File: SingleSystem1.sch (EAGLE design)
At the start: 7 parts, among them U2 SD_CARD_SOCKET, U3 XBEE

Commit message: done, now verifying
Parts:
- added 12+, GND: SE14, solpad:SE14
- added 3.3V, 5V, 9V: (no value), con-amp-quick:M02
- added 3DR: 653006114822, Wire_to_Board_Connectors_rev15d:653006114822
- added 5REG, 9REG: V_REG_317SMD, SparkFun-PowerIC:V_REG_317SMD
- added A1_FTDI, A2_FTDI, GPS_FTDI, IMU_FTDI: (no value), con-amp-quick:M06
- added ANEMOMETER1, ANEMOMETER2: 61200622323, Wurth_Elektronik_Electromechanic_Wire_to_Board_Connectors_rev15c:61200622323
- added C1, C3: 1uF, SparkFun-Capacitors:1UF-25V-10%(0805)
- added C13, C15: 0.1UF, SparkFun-Capacitors:1UF-25V-10%(0805)
- added C14, C16: 1UF, SparkFun-Capacitors:1UF-25V-10%(0805)
- added C2: 100uF, SparkFun-Capacitors:CAP1206
- added C4: 10uF, SparkFun-Capacitors:CAP0805
- added C5, C9: 0.022uF, SparkFun-Capacitors:CAP0603-CAP
- added D2: (no value), Wuerth_Elektronik_LEDs_rev15b:WL-SMCW-150120BS75000-B
- added R13: 68.1k, resistor:R-US_M2012
- added R17: 100k, resistor:R-US_M2012
- added R2: (no value), resistor:R-US_M2012
- added R3: 750 ohms, adafruit:R-US_M2012
- added R4, R6: 240 ohms, adafruit:R-US_M2012
- added R5: 1.5k, adafruit:R-US_M2012
- added R7: 1.07k, resistor:R-US_M2012
- added R8: 5.62k, resistor:R-US_M2012
- added R9: 11.8k, resistor:R-US_M2012
- added U1: LMZ14203, SparkFun-PowerIC:LMZ14203
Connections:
- new net +12V: 12+.MP, 9REG.IN, C1.1, C15.1, C4.1, D2.A, R13.2, R17.2, U1.VIN
- new net +9V: 5REG.IN, 9REG.OUT, 9V.2, C13.1, C16.1, R6.2, U$1.VIN
- new net 3DR_RX: 3DR.3
- new net 3DR_TX: 3DR.2
- new net A1_PWR: ANEMOMETER1.2
- new net A2_PWR: ANEMOMETER2.2
- new net N$2: 5REG.ADJ, R3.2, R4.1
- new net N$3: 9REG.ADJ, R5.2, R6.1
- new net N$4: R13.1, R9.2, U1.EN
- new net N$5: R17.1, U1.RON
- new net N$6: C9.1, U1.SS
- new net N$7: D2.K, R2.2
- new net N$8: C5.1, R7.2, R8.2, U1.FB
- net +5V: now also 3DR.1, 5REG.OUT, 5V.2, C14.1, R4.2
- net 3.3V: now also 3.3V.2, C2.1, C3.1, C5.2, R8.1, U1.VOUT
- net A1_IN_RX: now also ANEMOMETER1.5
- net A1_IN_TX: now also ANEMOMETER1.3
- net A1_RX: now also A1_FTDI.2
- net A1_TX: now also A1_FTDI.3
- net A2_IN_RX: now also ANEMOMETER2.5
- net A2_IN_TX: now also ANEMOMETER2.3
- net A2_RX: now also A2_FTDI.2
- net A2_TX: now also A2_FTDI.3
- net GND: now also 3.3V.1, 3DR.6, 5V.1, 9V.1, A1_FTDI.6, A2_FTDI.6, ANEMOMETER1.1, ANEMOMETER1.4, ANEMOMETER2.1, ANEMOMETER2.4, C1.2, C13.2, C14.2, C15.2, C16.2, C2.2, C3.2, C4.2, C9.2, GND.MP, GPS_FTDI.6, IMU_FTDI.6, R2.1, R3.1, R5.1, R7.1, R9.1, U$1.5V, U1.EP, U1.GND
- net GPS_RX: now also GPS_FTDI.3, U$1.52
- net GPS_TX: now also GPS_FTDI.2, U$1.A11
- net IMU_RX: now also IMU_FTDI.3
- net IMU_TX: now also IMU_FTDI.2

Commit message: Done, Kanishke will verify
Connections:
- net GND: now also U$1.GND_1; no longer U$1.5V
- net GPS_RX: now also U$1.A11; no longer U$1.52
- net GPS_TX: now also U$1.52; no longer U$1.A11
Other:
- moved on the sheet: GPS(OEM615), IMUCONNECTION, MAX232_1, MAX232_2, U2, U3

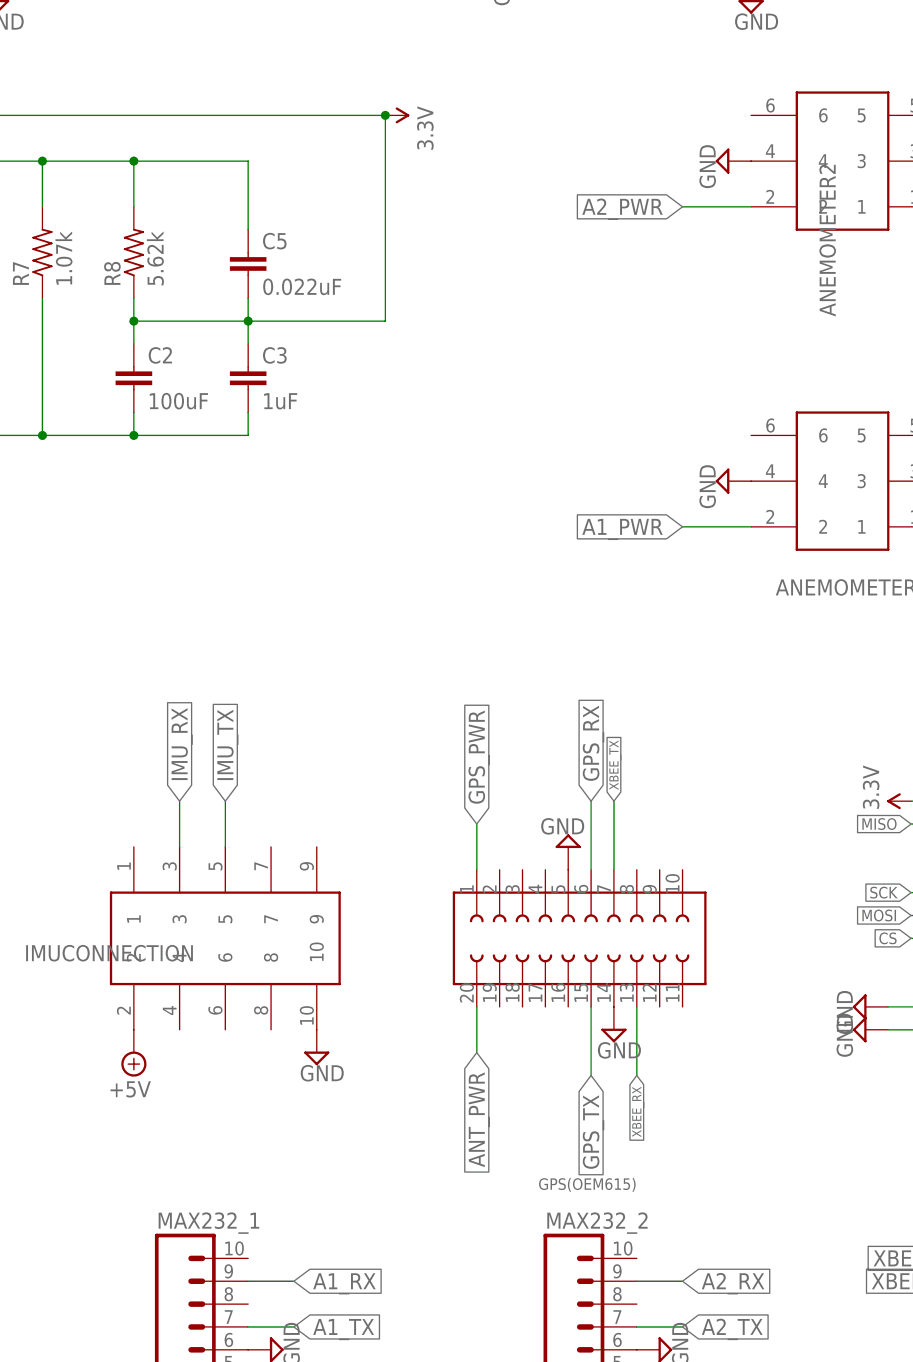
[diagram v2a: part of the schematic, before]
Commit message: edited the pwr connections
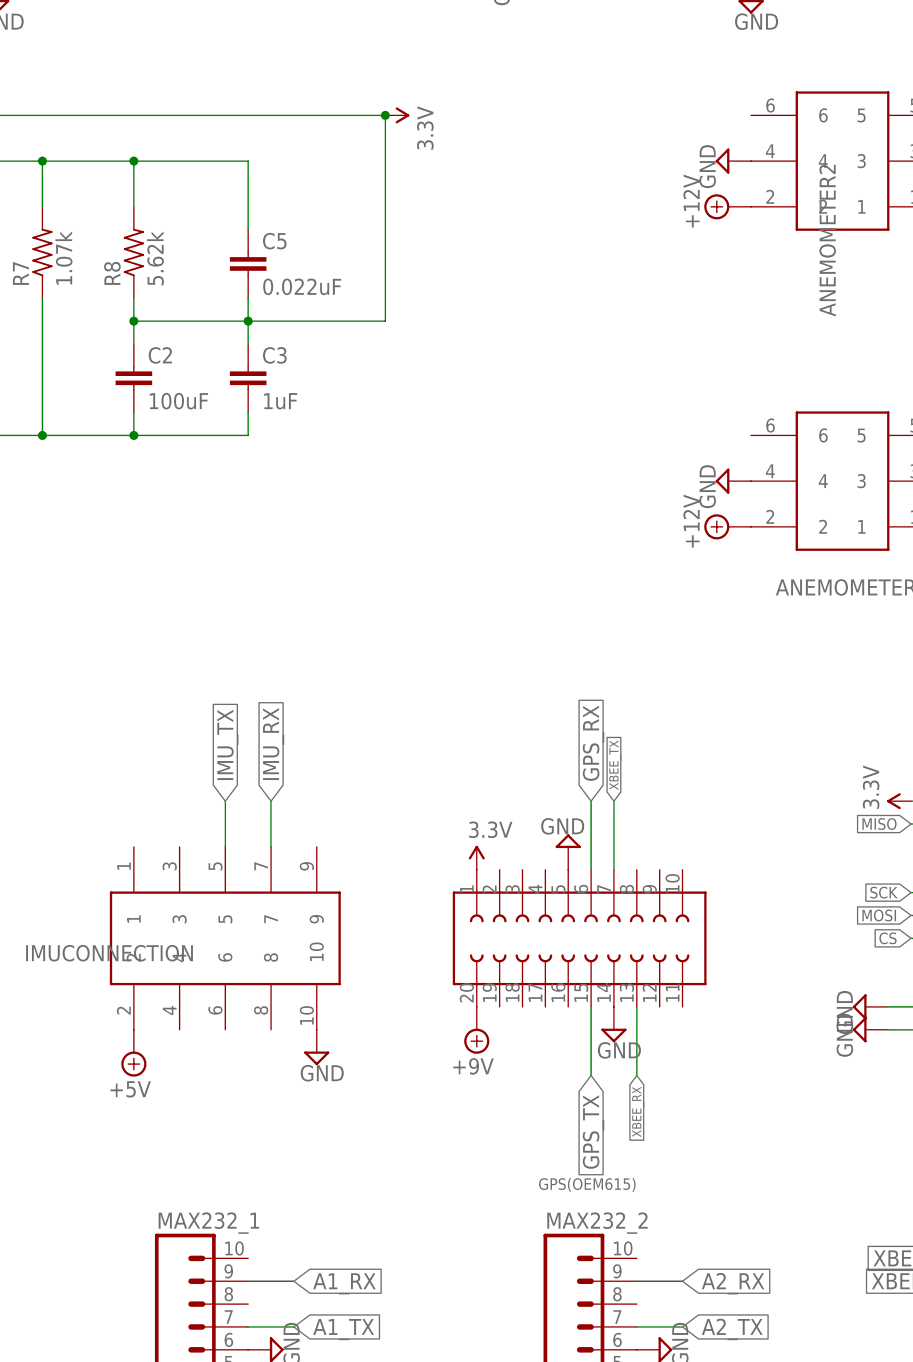
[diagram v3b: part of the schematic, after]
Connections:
- removed net A1_PWR: ANEMOMETER1.2
- removed net A2_PWR: ANEMOMETER2.2
- removed net ANT_PWR: GPS(OEM615).20
- removed net GPS_PWR: GPS(OEM615).1
- net +12V: now also ANEMOMETER1.2, ANEMOMETER2.2
- net +9V: now also GPS(OEM615).20
- net 3.3V: now also GPS(OEM615).1
- net IMU_RX: now also IMUCONNECTION.7; no longer IMUCONNECTION.3
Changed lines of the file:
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@@
 <part name="SUPPLY2" library="supply2" deviceset="+9V" device=""/>
 <part name="SUPPLY5" library="supply2" deviceset="GND" device=""/>
+<part name="SUPPLY6" library="supply2" deviceset="+9V" device=""/>
+<part name="SUPPLY7" library="SparkFun-Aesthetics" deviceset="3.3V" device=""/>
+<part name="SUPPLY10" library="supply2" deviceset="+12V" device=""/>
+<part name="SUPPLY17" library="supply2" deviceset="+12V" device=""/>
 </parts>
 <sheets>
@@
 <instance part="SUPPLY2" gate="G$1" x="2.54" y="15.24" rot="R90"/>
 <instance part="SUPPLY5" gate="GND" x="2.54" y="20.32" rot="R270"/>
+<instance part="SUPPLY6" gate="G$1" x="142.24" y="68.58" rot="R180"/>
+<instance part="SUPPLY7" gate="G$1" x="142.24" y="86.36"/>
+<instance part="SUPPLY10" gate="+12V" x="170.18" y="160.02" rot="R90"/>
+<instance part="SUPPLY17" gate="+12V" x="170.18" y="124.46" rot="R90"/>
 </instances>
 <busses>
@@
 <net name="IMU_RX" class="0">
 <segment>
-<pinref part="IMUCONNECTION" gate="G$1" pin="3"/>
-<wire x1="109.22" y1="88.9" x2="109.22" y2="93.98" width="0.1524" layer="91"/>
-<label x="109.22" y="93.98" size="1.778" layer="95" rot="R90" xref="yes"/>
-</segment>
-<segment>
 <pinref part="U$1" gate="G$1" pin="TX3"/>
 <wire x1="5.08" y1="68.58" x2="0" y2="68.58" width="0.1524" layer="91"/>
@@
 <label x="45.72" y="248.92" size="1.778" layer="95" xref="yes"/>
 </segment>
+<segment>
+<pinref part="IMUCONNECTION" gate="G$1" pin="7"/>
+<wire x1="119.38" y1="88.9" x2="119.38" y2="93.98" width="0.1524" layer="91"/>
+<label x="119.38" y="93.98" size="1.778" layer="95" rot="R90" xref="yes"/>
+</segment>
 </net>
 <net name="IMU_TX" class="0">
+<segment>
+<pinref part="U$1" gate="G$1" pin="RX3"/>
+<wire x1="5.08" y1="66.04" x2="0" y2="66.04" width="0.1524" layer="91"/>
+<label x="0" y="66.04" size="1.778" layer="95" rot="R180" xref="yes"/>
+</segment>
+<segment>
+<pinref part="IMU_FTDI" gate="G$1" pin="2"/>
+<wire x1="35.56" y1="246.38" x2="45.72" y2="246.38" width="0.1524" layer="91"/>
+<label x="45.72" y="246.38" size="1.778" layer="95" xref="yes"/>
+</segment>
 <segment>
 <pinref part="IMUCONNECTION" gate="G$1" pin="5"/>
@@
 <label x="114.3" y="93.98" size="1.778" layer="95" rot="R90" xref="yes"/>
 </segment>
-<segment>
-<pinref part="U$1" gate="G$1" pin="RX3"/>
-<wire x1="5.08" y1="66.04" x2="0" y2="66.04" width="0.1524" layer="91"/>
-<label x="0" y="66.04" size="1.778" layer="95" rot="R180" xref="yes"/>
-</segment>
-<segment>
-<pinref part="IMU_FTDI" gate="G$1" pin="2"/>
-<wire x1="35.56" y1="246.38" x2="45.72" y2="246.38" width="0.1524" layer="91"/>
-<label x="45.72" y="246.38" size="1.778" layer="95" xref="yes"/>
-</segment>
 </net>
 <net name="XBEE_TX" class="0">
@@
 <pinref part="U3" gate="G$1" pin="DIN"/>
 <label x="198.12" y="40.64" size="1.778" layer="95" rot="R180" xref="yes"/>
-</segment>
-</net>
-<net name="GPS_PWR" class="0">
-<segment>
-<pinref part="GPS(OEM615)" gate="G$1" pin="1"/>
-<wire x1="142.24" y1="86.36" x2="142.24" y2="91.44" width="0.1524" layer="91"/>
-<label x="142.24" y="91.44" size="1.778" layer="95" rot="R90" xref="yes"/>
-</segment>
-</net>
-<net name="ANT_PWR" class="0">
-<segment>
-<pinref part="GPS(OEM615)" gate="G$1" pin="20"/>
-<wire x1="142.24" y1="71.12" x2="142.24" y2="66.04" width="0.1524" layer="91"/>
-<label x="142.24" y="66.04" size="1.778" layer="95" rot="R270" xref="yes"/>
 </segment>
 </net>
@@
 <pinref part="3.3V" gate="G$1" pin="2"/>
 <pinref part="SUPPLY22" gate="G$1" pin="3.3V"/>
+</segment>
+<segment>
+<pinref part="GPS(OEM615)" gate="G$1" pin="1"/>
+<pinref part="SUPPLY7" gate="G$1" pin="3.3V"/>
 </segment>
 </net>
@@
 <pinref part="SUPPLY21" gate="+12V" pin="+12V"/>
 </segment>
+<segment>
+<pinref part="ANEMOMETER2" gate="G$1" pin="2"/>
+<pinref part="SUPPLY10" gate="+12V" pin="+12V"/>
+</segment>
+<segment>
+<pinref part="ANEMOMETER1" gate="G$1" pin="2"/>
+<pinref part="SUPPLY17" gate="+12V" pin="+12V"/>
+</segment>
 </net>
 <net name="N$4" class="0">
@@
 <pinref part="SUPPLY2" gate="G$1" pin="+9V"/>
 </segment>
+<segment>
+<pinref part="GPS(OEM615)" gate="G$1" pin="20"/>
+<pinref part="SUPPLY6" gate="G$1" pin="+9V"/>
+</segment>
 </net>
 <net name="N$2" class="0">
@@
 </segment>
 </net>
-<net name="A1_PWR" class="0">
-<segment>
-<pinref part="ANEMOMETER1" gate="G$1" pin="2"/>
-<wire x1="172.72" y1="124.46" x2="165.1" y2="124.46" width="0.1524" layer="91"/>
-<label x="165.1" y="124.46" size="1.778" layer="95" rot="R180" xref="yes"/>
-</segment>
-</net>
-<net name="A2_PWR" class="0">
-<segment>
-<pinref part="ANEMOMETER2" gate="G$1" pin="2"/>
-<wire x1="172.72" y1="160.02" x2="165.1" y2="160.02" width="0.1524" layer="91"/>
-<label x="165.1" y="160.02" size="1.778" layer="95" rot="R180" xref="yes"/>
-</segment>
-</net>

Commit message: edited 3DR
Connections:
- net 3DR_RX: now also U$1.TX0
- net 3DR_TX: now also U$1.RX0
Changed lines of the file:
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@@
 <wire x1="33.02" y1="208.28" x2="33.02" y2="198.12" width="0.1524" layer="91"/>
+</segment>
+<segment>
+<pinref part="U$1" gate="G$1" pin="TX0"/>
+<wire x1="5.08" y1="53.34" x2="0" y2="53.34" width="0.1524" layer="91"/>
+<label x="0" y="53.34" size="1.778" layer="95" rot="R180" xref="yes"/>
 </segment>
 </net>
@@
 <wire x1="27.94" y1="210.82" x2="27.94" y2="198.12" width="0.1524" layer="91"/>
 </segment>
+<segment>
+<pinref part="U$1" gate="G$1" pin="RX0"/>
+<wire x1="5.08" y1="50.8" x2="0" y2="50.8" width="0.1524" layer="91"/>
+<label x="0" y="50.8" size="1.778" layer="95" rot="R180" xref="yes"/>
+</segment>
 </net>
